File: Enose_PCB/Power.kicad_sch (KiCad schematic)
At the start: 54 parts, among them IC1 ISL91127IRNZ-T7A, IC2 MP2722GRH-0000-Z, J5 USB_C_Receptacle_USB2.0_16P, J6 Battery Terminal, SW3 SW_SPST, U2 USBLC6-4SC6

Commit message: Changed power symbols
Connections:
- net BATT is gone; now on net +BATT: C24.2, IC2.12 (BATTSNS), IC2.14 (BATT), J6.1 (Pin_1)
- net +BATT: no longer C11.1, C12.1, C7.1, IC1.10 (VIN), IC1.11 (EN), IC1.6 (PVIN_1), IC1.7 (PVIN_2), IC1.8 (PVIN_3), IC1.9 (PVIN_4), L3.1, PS1.7 (VIN)
- net +SYS: no longer R7.1
- new net +SYS_SW: C11.1, C12.1, C7.1, IC1.10 (VIN), IC1.11 (EN), IC1.6 (PVIN_1), IC1.7 (PVIN_2), IC1.8 (PVIN_3), IC1.9 (PVIN_4), L3.1, PS1.7 (VIN), R7.1
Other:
- moved on the sheet: C24, J6, SW3

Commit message: Added something idk
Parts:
- TH1: footprint (none) -> Connector_JST:JST_XH_B2B-XH-AM_1x02_P2.50mm_Vertical
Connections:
- net VBUS: no longer C17.1, C18.2, IC2.2 (IN), J5.A4 (VBUS), J5.A9 (VBUS), J5.B4 (VBUS), J5.B9 (VBUS), U2.5 (VBUS)
- new net +VBUS: C17.1, C18.2, IC2.2 (IN), J5.A4 (VBUS), J5.A9 (VBUS), J5.B4 (VBUS), J5.B9 (VBUS), U2.5 (VBUS)
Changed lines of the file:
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@@
 			)
 		)
-		(property "Value" "VBUS"
+		(property "Value" "+VBUS"
 			(at 182.88 111.7599 90)
 			(effects
@@
 			)
 		)
-		(property "Footprint" ""
+		(property "Footprint" "Connector_JST:JST_XH_B2B-XH-AM_1x02_P2.50mm_Vertical"
 			(at 120.65 100.33 0)
 			(effects
@@
 			)
 		)
-		(property "Value" "VBUS"
+		(property "Value" "+VBUS"
 			(at 95.25 29.2099 90)
 			(effects

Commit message: Working on Enose PCB Layout
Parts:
- added C42: 100nF, Capacitor_SMD:C_0805_2012Metric_Pad1.18x1.45mm_HandSolder, symbol Device:C
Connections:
- net GND: now also C42.1
- net NTC1: now also C42.2
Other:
- moved on the sheet: TP3

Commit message: Enose PCB almost done
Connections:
- net LX2: now reaches IC1.1 (LX2_1), IC1.2 (LX2_2), L1.1
- net LX1: now reaches IC1.4 (LX1_1), IC1.5 (LX1_2), L1.2
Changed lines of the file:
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@@
+		)
+	)
+	(label "LX2"
+		(at 33.02 132.08 0)
+		(effects
+			(font
+				(size 1.27 1.27)
+			)
+			(justify left bottom)
 		)
 	)
@@
 		(effects
 			(font
+				(size 1.27 1.27)
+			)
+			(justify left bottom)
+		)
+	)
+	(label "LX1"
+		(at 33.02 139.7 0)
+		(effects
+			(font

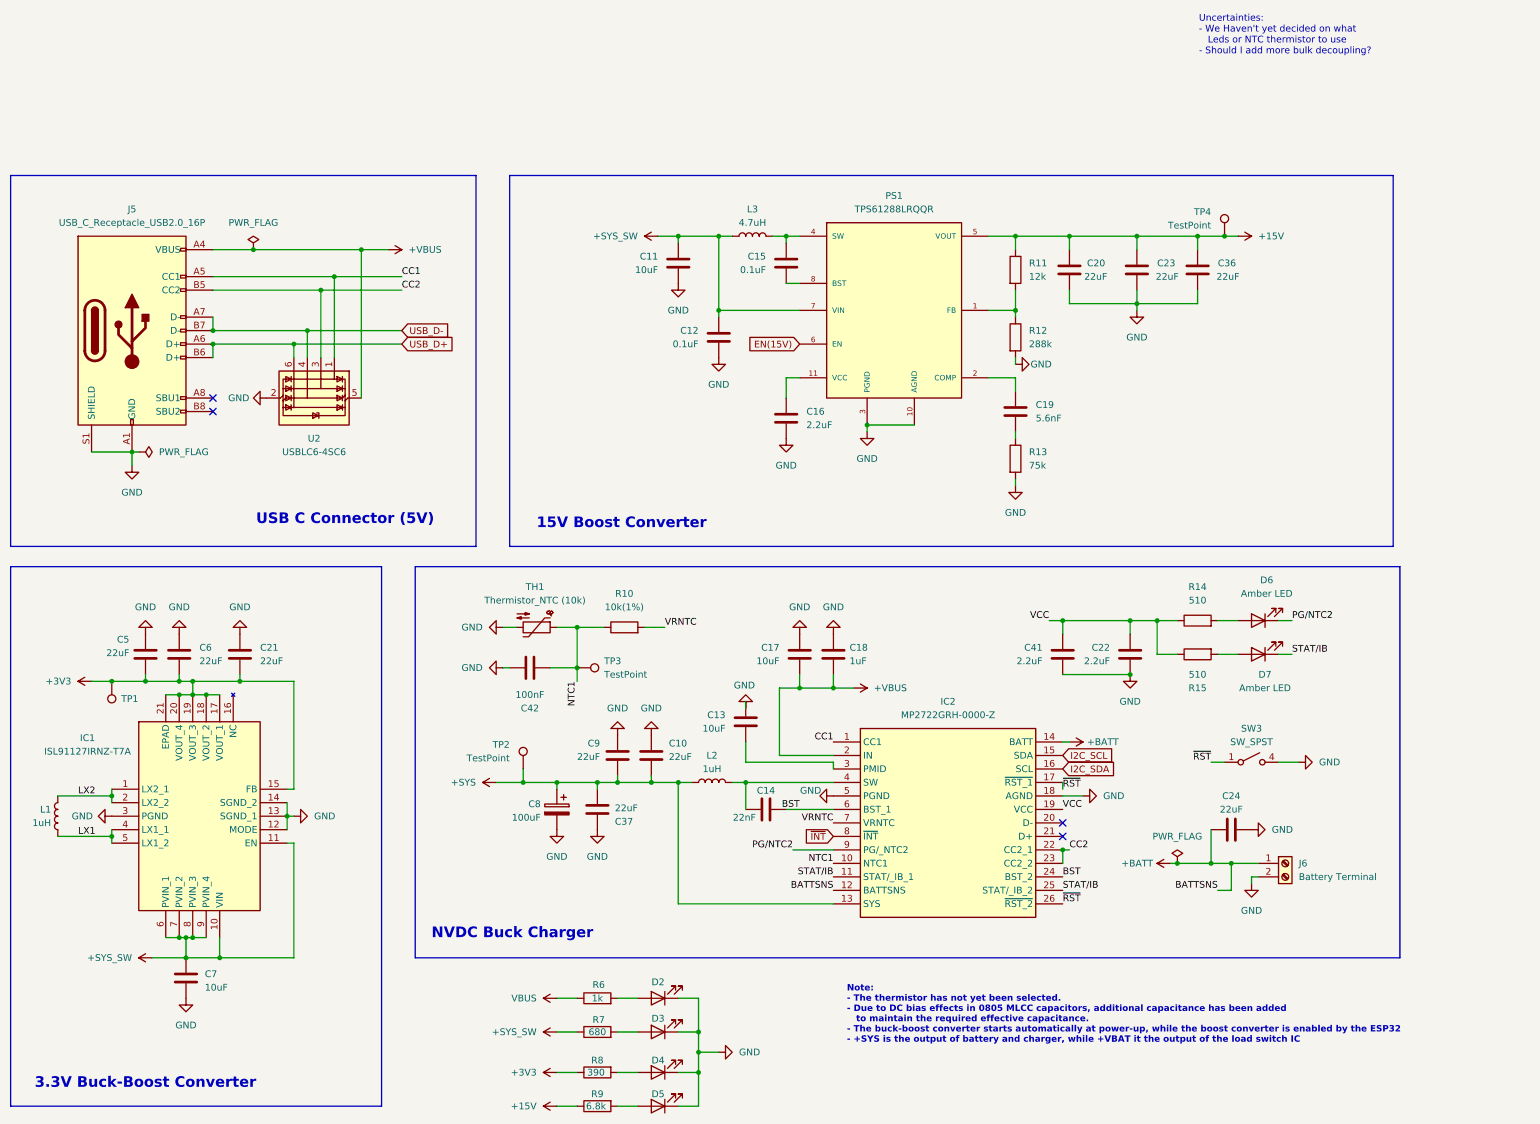
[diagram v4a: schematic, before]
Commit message: Enose PCB almost done, just needs ground vias
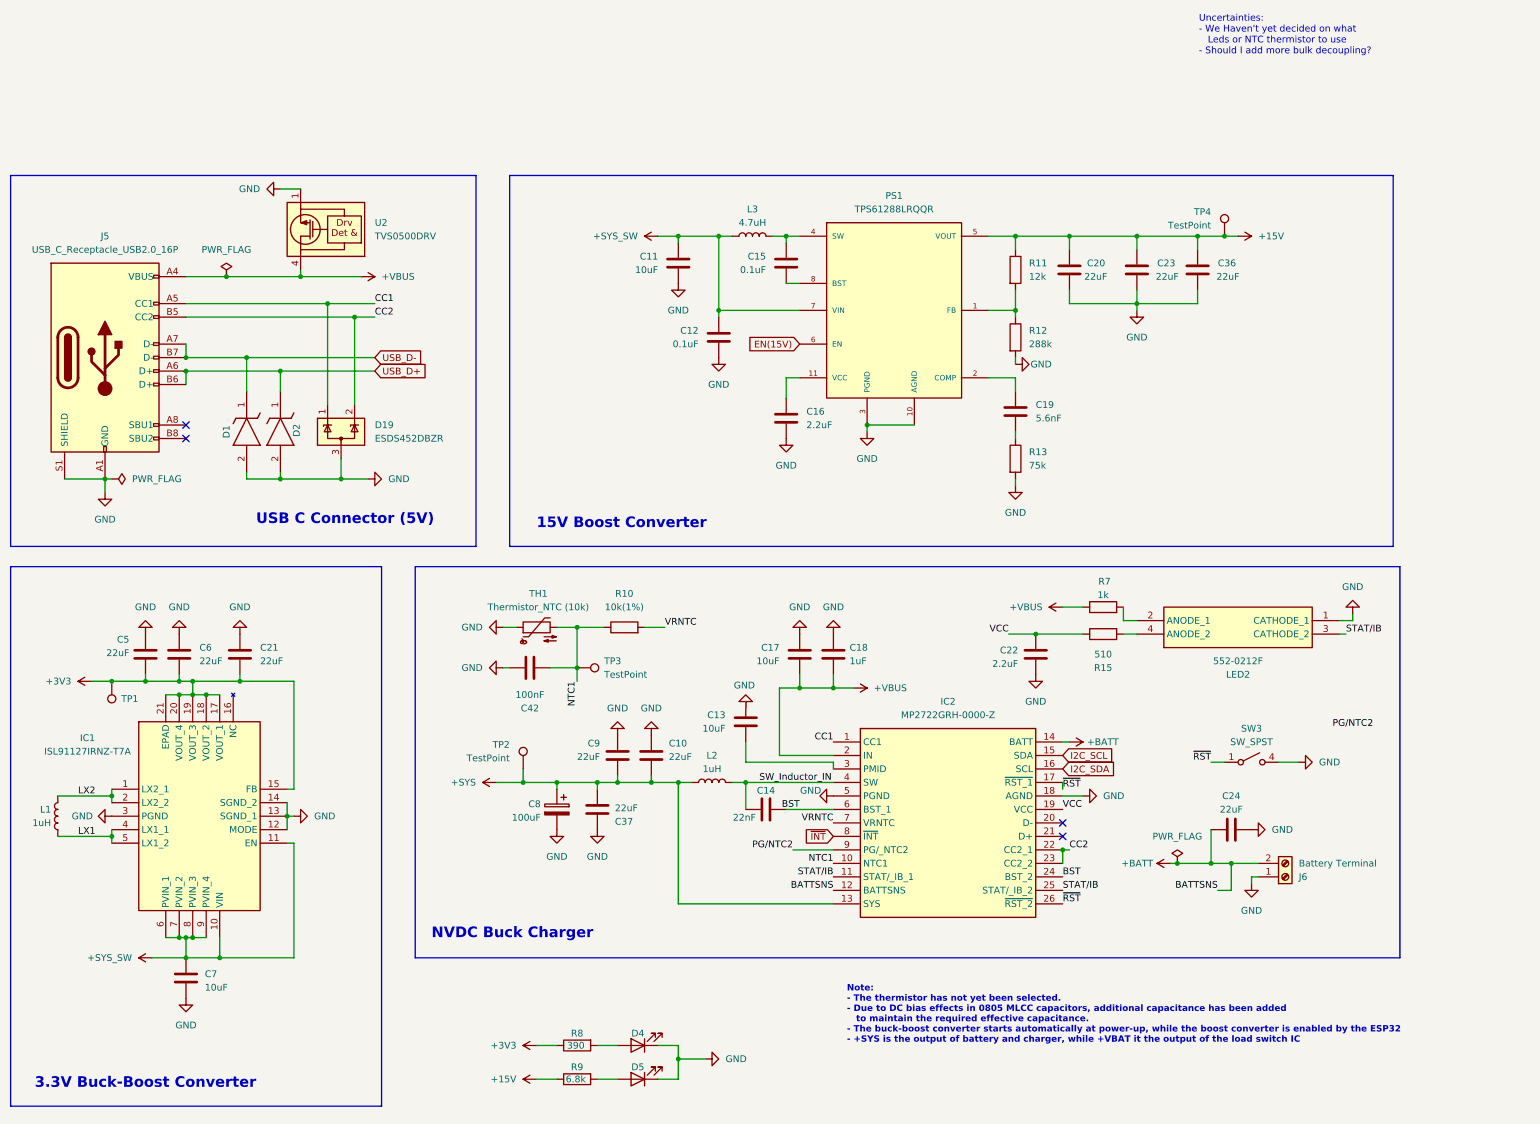
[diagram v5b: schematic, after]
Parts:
- removed C41: 2.2uF, Capacitor_SMD:C_0805_2012Metric_Pad1.18x1.45mm_HandSolder, symbol Device:C
- removed D2, D3: LED, LED_SMD:LED_0805_2012Metric_Pad1.15x1.40mm_HandSolder, symbol Device:LED
- removed D6, D7: Amber LED, LED_SMD:LED_0805_2012Metric_Pad1.15x1.40mm_HandSolder, symbol Device:LED
- removed R14: 510, Resistor_SMD:R_0805_2012Metric_Pad1.20x1.40mm_HandSolder, symbol Device:R
- removed R6: 1k, Resistor_SMD:R_0805_2012Metric_Pad1.20x1.40mm_HandSolder, symbol Device:R
- removed U2: USBLC6-4SC6, Package_TO_SOT_SMD:SOT-23-6_Handsoldering, symbol Power_Protection:USBLC6-4SC6
- added D1, D2: ESD8351XV2T1G, SamacSys_Parts:SODFL1608X70N, symbol SamacSys_Parts:ESD8351XV2T1G
- added D19: ESDS452DBZR, Package_TO_SOT_SMD:SOT-23-3, symbol Power_Protection:SP0502BAJT
- added LED2: 552-0212F, SamacSys_Parts:5520212F, symbol SamacSys_Parts:552-0212F
- added U2: TVS0500DRV, Package_SON:WSON-6-1EP_2x2mm_P0.65mm_EP1x1.6mm, symbol Power_Protection:TVS0500DRV
- R7: value 680 -> 1k
- TP1, TP2, TP3, TP4: footprint TestPoint:TestPoint_Pad_1.5x1.5mm -> TestPoint:TestPoint_Pad_D1.5mm
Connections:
- net +BATT: now also J6.2 (Pin_2); no longer J6.1 (Pin_1)
- net +SYS_SW: no longer R7.1
- net +VBUS: now also R7.1, U2.4 (IN), U2.5 (IN), U2.6 (IN)
- net CC1: now also D19.1 (K)
- net CC2: now also D19.2 (K)
- net GND: now also J6.1 (Pin_1), TH1.1, D1.2 (A), D19.3 (A), D2.2 (A), LED2.1 (CATHODE_1), U2.1 (GND), U2.2 (GND), U2.3 (GND), U2.7 (GND); no longer J6.2 (Pin_2), TH1.2
- net NTC1: now also TH1.2; no longer TH1.1
- net STAT/IB: now also LED2.3 (CATHODE_2)
- net USB_D+: now also D2.1 (K)
- net USB_D-: now also D1.1 (K)
- net at R15.2: now also LED2.4 (ANODE_2)
- net SW_Inductor_IN: now reaches C14.1, IC2.4 (SW), L2.2
- net at R7.2: now also LED2.2 (ANODE_1)
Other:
- moved on the sheet: C22, D4, D5, J5, R15, R8, R9, TH1

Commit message: Enose board ready for review
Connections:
- net +VBUS: now also TP3.1
- net NTC1: no longer TP3.1
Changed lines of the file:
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@@
 	)
 	(junction
+		(at 83.82 34.29)
+		(diameter 0)
+		(color 0 0 0 0)
+	)
+	(junction
 		(at 246.38 144.78)
 		(diameter 0)
@@
 	(wire
 		(pts
+			(xy 83.82 34.29) (xy 86.36 34.29)
+		)
+		(stroke
+			(width 0)
+			(type default)
+		)
+	)
+	(wire
+		(pts
 			(xy 259.08 125.73) (xy 262.89 125.73)
 		)
@@
 	(wire
 		(pts
-			(xy 74.93 34.29) (xy 86.36 34.29)
+			(xy 74.93 34.29) (xy 83.82 34.29)
 		)
 		(stroke
@@
 	)
 	(label "PG{slash}NTC2"
-		(at 269.24 119.38 0)
+		(at 266.7 114.3 0)
 		(effects
 			(font
@@
 	)
 	(symbol
-		(lib_id "Connector:TestPoint")
-		(at 127 107.95 270)
-		(unit 1)
-		(exclude_from_sim no)
-		(in_bom yes)
-		(on_board yes)
-		(dnp no)
-		(fields_autoplaced yes)
-		(property "Reference" "TP3"
-			(at 132.08 106.6799 90)
-			(effects
-				(font
-					(size 1.27 1.27)
-				)
-				(justify left)
-			)
-		)
-		(property "Value" "TestPoint"
-			(at 132.08 109.2199 90)
-			(effects
-				(font
-					(size 1.27 1.27)
-				)
-				(justify left)
-			)
-		)
-		(property "Footprint" "TestPoint:TestPoint_Pad_D1.5mm"
-			(at 127 113.03 0)
-			(effects
-				(font
-					(size 1.27 1.27)
-				)
-				(hide yes)
-			)
-		)
-		(property "Datasheet" "~"
-			(at 127 113.03 0)
-			(effects
-				(font
-					(size 1.27 1.27)
-				)
-				(hide yes)
-			)
-		)
-		(property "Description" "test point"
-			(at 127 107.95 0)
-			(effects
-				(font
-					(size 1.27 1.27)
-				)
-				(hide yes)
-			)
-		)
-		(pin "1"
-		)
-		(instances
-			(project ""
-				(path "/eef70be0-4107-491c-8ca0-465071a6397e/c704ca63-8ab0-46ce-942e-504221cfea41"
-					(reference "TP3")
-					(unit 1)
-				)
-			)
-		)
-	)
-	(symbol
 		(lib_id "Device:L")
 		(at 29.21 135.89 0)
@@
 					(unit 1)
 				)
+			)
+		)
+	)
+	(symbol
+		(lib_id "Connector:TestPoint")
+		(at 83.82 34.29 0)
+		(mirror x)
+		(unit 1)
+		(exclude_from_sim no)
+		(in_bom yes)
+		(on_board yes)
+		(dnp no)
+		(property "Reference" "TP3"
+			(at 78.74 37.338 0)
+			(effects
+				(font
+					(size 1.27 1.27)
+				)
+				(justify left)
+			)
+		)
+		(property "Value" "TestPoint"
+			(at 86.36 36.3221 0)
+			(effects
+				(font
+					(size 1.27 1.27)
+				)
+				(justify left)
+				(hide yes)
+			)
+		)
+		(property "Footprint" "TestPoint:TestPoint_Pad_D1.5mm"
+			(at 88.9 34.29 0)
+			(effects
+				(font
+					(size 1.27 1.27)
+				)
+				(hide yes)
+			)
+		)
+		(property "Datasheet" "~"
+			(at 88.9 34.29 0)
+			(effects
+				(font
+					(size 1.27 1.27)
+				)
+				(hide yes)
+			)
+		)
+		(property "Description" "test point"
+			(at 83.82 34.29 0)
+			(effects
+				(font
+					(size 1.27 1.27)
+				)
+				(hide yes)
+			)
+		)
+		(pin "1"
+		)
+		(instances
+			(project "Enose_PCB"
+				(path "/eef70be0-4107-491c-8ca0-465071a6397e/c704ca63-8ab0-46ce-942e-504221cfea41"
+					(reference "TP3")
+					(unit 1)
+				)

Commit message: Enose PCB finished
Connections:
- net PG/NTC2: no longer names the net of IC2.9 (PG/_NTC2)
- no-connect marks 4 -> 5
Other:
- note removed: "Uncertainties: - We Haven't yet decided on what Leds or NTC thermistor to use - Should I add more bulk decoupling?"
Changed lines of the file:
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@@
-		)
-	)
-	(text "Uncertainties:\n- We Haven't yet decided on what \n   Leds or NTC thermistor to use\n- Should I add more bulk decoupling?\n"
-		(exclude_from_sim no)
-		(at 244.094 -11.176 0)
-		(effects
-			(font
-				(size 1.27 1.27)
-			)
-			(justify left)
 		)
 	)
@@
 	)
 	(no_connect
+		(at 175.26 142.24)
+	)
+	(no_connect
 		(at 218.44 139.7)
 	)
@@
 		(pts
 			(xy 53.34 52.07) (xy 71.12 52.07)
-		)
-		(stroke
-			(width 0)
-			(type default)
-		)
-	)
-	(wire
-		(pts
-			(xy 167.64 142.24) (xy 175.26 142.24)
 		)
 		(stroke
@@
 		)
 	)
-	(label "PG{slash}NTC2"
-		(at 167.64 142.24 180)
-		(effects
-			(font
-				(size 1.27 1.27)
-			)
-			(justify right bottom)
-		)
-	)
 	(label "BATTSNS"
 		(at 175.26 149.86 180)
@@
 		)
 	)
-	(label "PG{slash}NTC2"
-		(at 266.7 114.3 0)
-		(effects
-			(font
-				(size 1.27 1.27)
-			)
-			(justify left bottom)
-		)
-	)
